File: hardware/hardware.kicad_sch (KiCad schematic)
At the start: 28 parts, among them J1 Conn_01x02, J2 Conn_01x02, P1 USB_C_Plug, Q1 BSS138, Q2 BSS138, U1 ATmega328-P, U3 LM1117S-3.3, U4 CH340C, Y1 Crystal_GND24

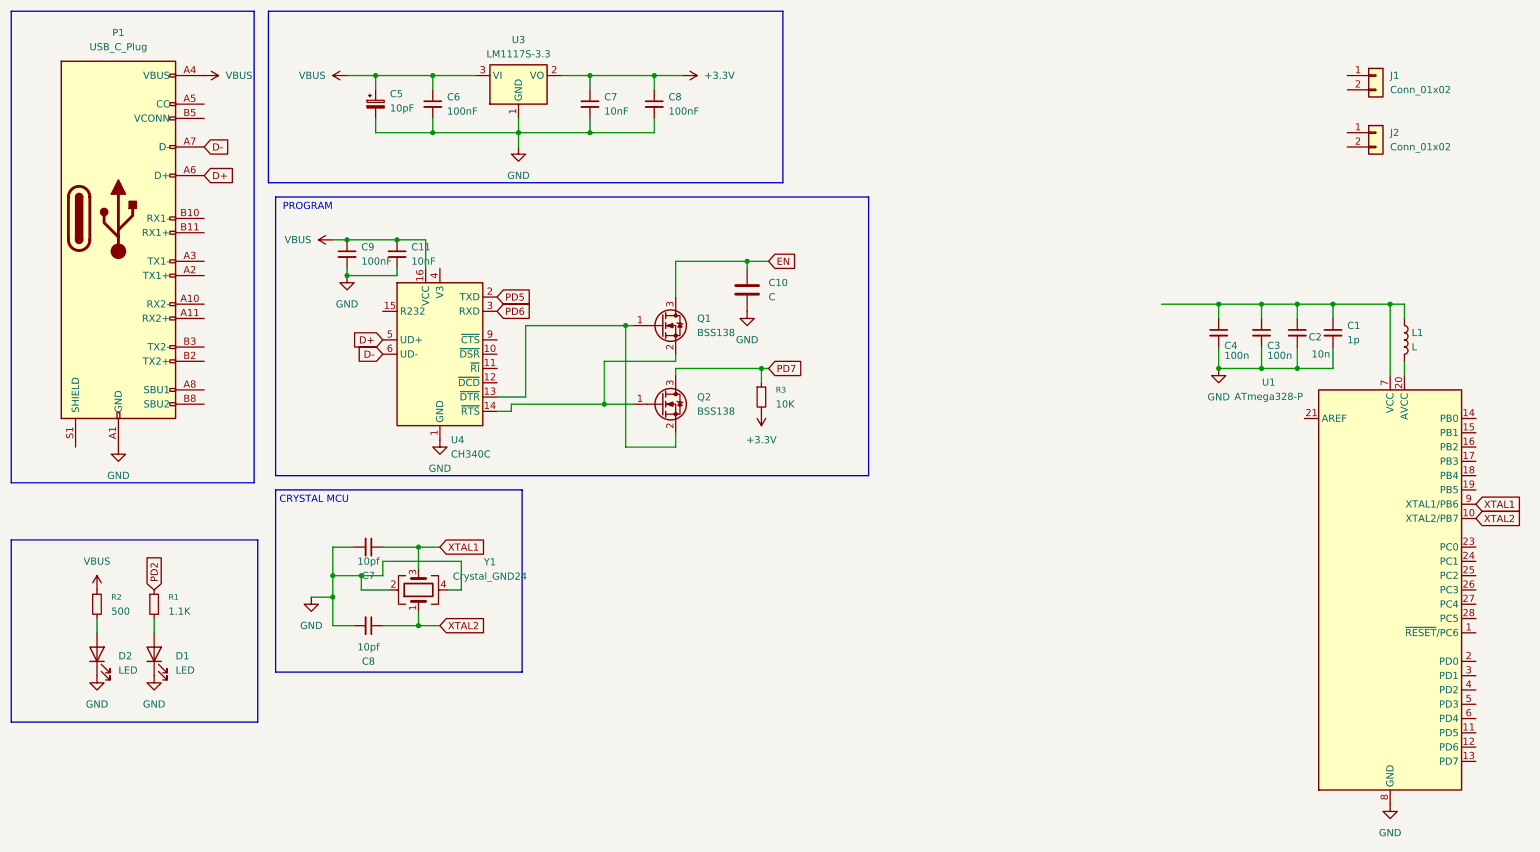
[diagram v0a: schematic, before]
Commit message: add qfn32 atmega
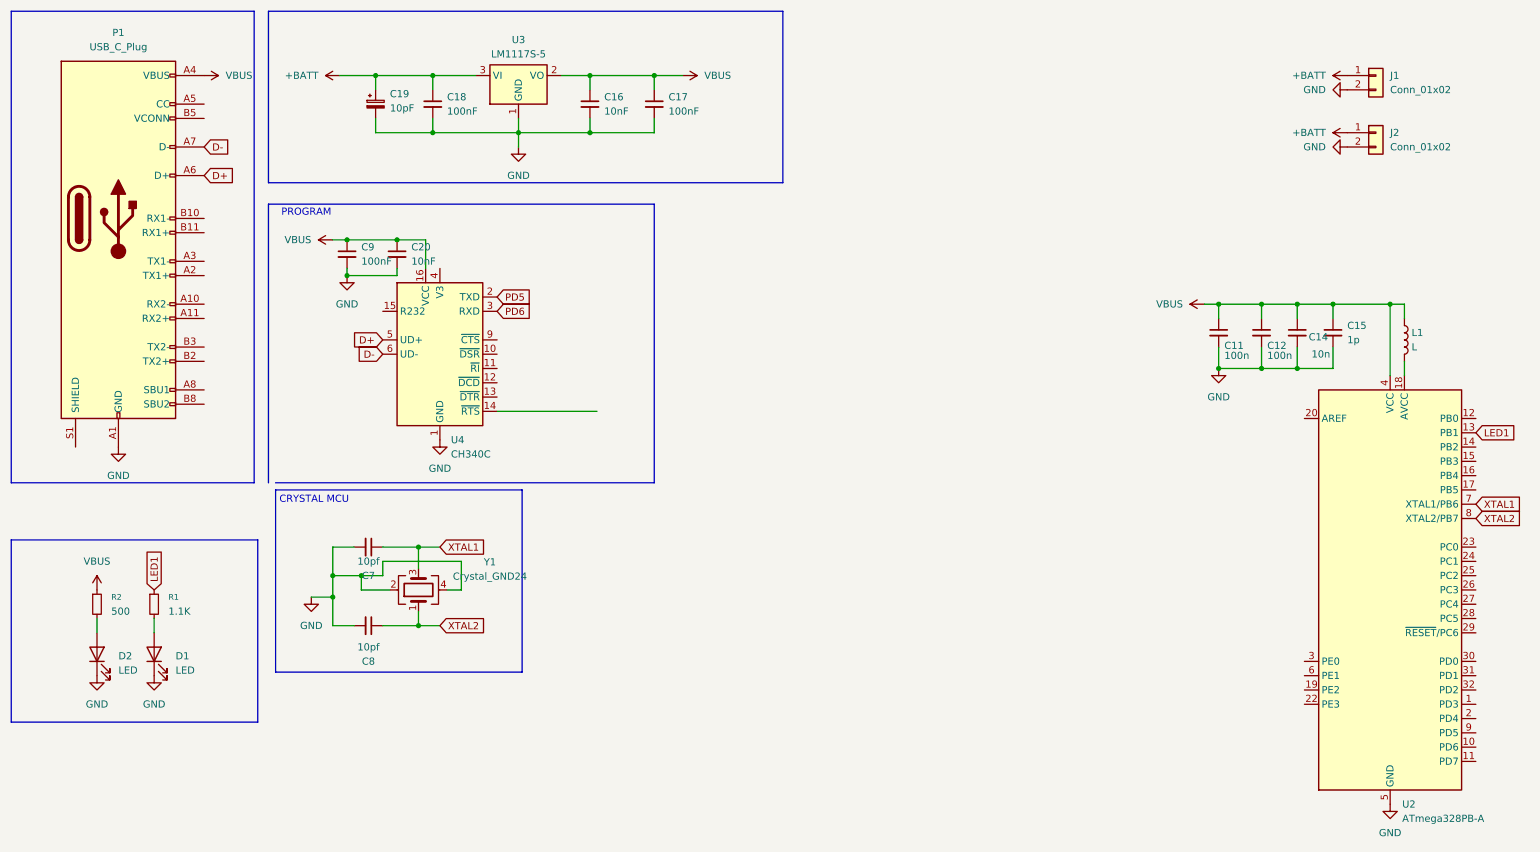
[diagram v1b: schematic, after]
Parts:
- removed C10: C, Capacitor_SMD:C_0603_1608Metric, symbol Device:C
- removed Q1, Q2: BSS138, Package_TO_SOT_SMD:SOT-23, symbol Transistor_FET:BSS138
- removed R3: 10K, Resistor_SMD:R_0603_1608Metric, symbol Device:R_Small
- removed U1: ATmega328-P, Package_DIP:DIP-28_W7.62mm, symbol MCU_Microchip_ATmega:ATmega328-P
- added U2: ATmega328PB-A, Package_QFP:TQFP-32_7x7mm_P0.8mm, symbol MCU_Microchip_ATmega:ATmega328PB-A
- U3: value LM1117S-3.3 -> LM1117S-5
- renumbered C4 to C11, C3 to C12, C2 to C14, C1 to C15, C7 to C16, C8 to C17, C6 to C18, C5 to C19, C11 to C20
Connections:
- net +3.3V is gone; now on net VBUS: C16.1, C17.1, U3.2 (VO)
- net GND: now also J1.2 (Pin_2), J2.2 (Pin_2), U2.21 (GND), U2.5 (GND)
- net VBUS: now also C11.1, C12.1, C14.1, C15.1, L1.1, U2.4 (VCC); no longer C18.1, C19.1, U3.3 (VI)
- net XTAL1: now also U2.7 (XTAL1/PB6)
- net XTAL2: now also U2.8 (XTAL2/PB7)
- net +BATT: now reaches J2.1 (Pin_1)
- net +BATT: now also C18.1, C19.1, J1.1 (Pin_1), U3.3 (VI)
- net at L1.2: now also U2.18 (AVCC)
- net PD2 renamed LED1
- net LED1: now also U2.13 (PB1)

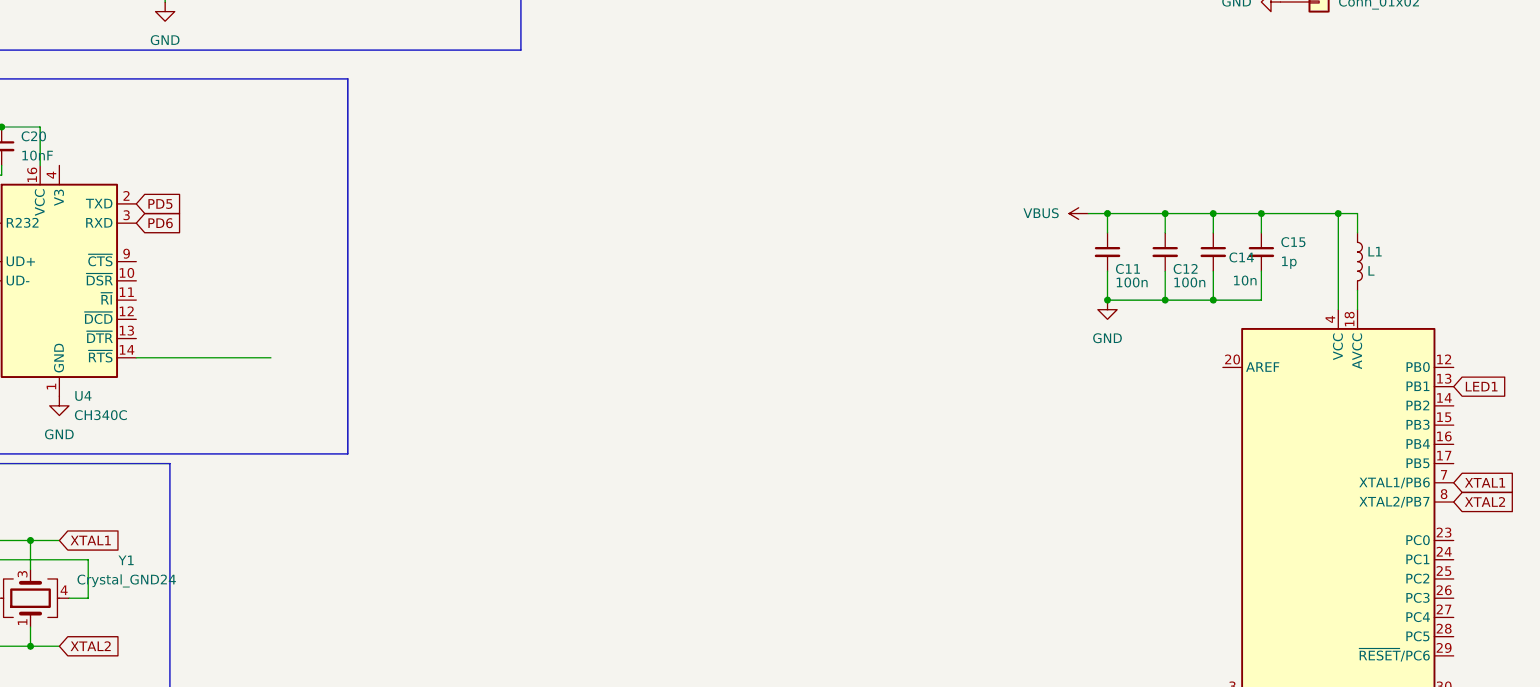
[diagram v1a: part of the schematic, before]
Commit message: add isp connector
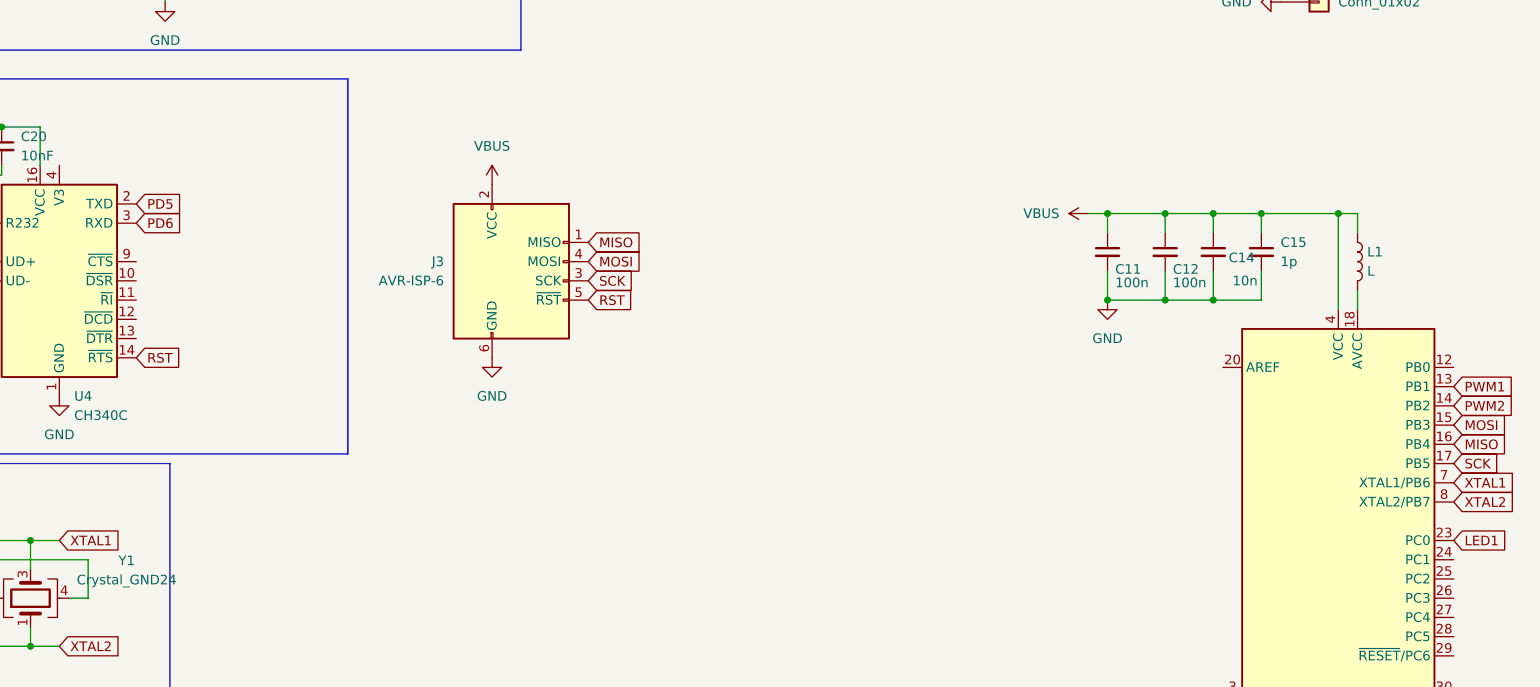
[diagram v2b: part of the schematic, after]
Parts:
- added J3: AVR-ISP-6, Connector_PinHeader_2.54mm:PinHeader_2x03_P2.54mm_Vertical, symbol Connector:AVR-ISP-6
- C11, C12, C14, C15: footprint (none) -> Capacitor_SMD:C_0603_1608Metric
- L1: footprint (none) -> Inductor_SMD:L_0603_1608Metric
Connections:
- net GND: now also J3.6 (GND)
- net LED1: now also U2.23 (PC0); no longer U2.13 (PB1)
- net VBUS: now also J3.2 (VCC)
- net PWM2: now reaches U2.14 (PB2)
- net MOSI: now reaches U2.15 (PB3)
- net MOSI: now also J3.4 (MOSI)
- net MISO: now reaches U2.16 (PB4)
- net MISO: now also J3.1 (MISO)
- net SCK: now reaches U2.17 (PB5)
- net SCK: now also J3.3 (SCK)
- net RST: now reaches U4.14 (~{RTS})
- net RST: now also J3.5 (~{RST})
- new net PWM1: U2.13 (PB1)

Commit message: finish schematic
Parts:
- added J4, J5: Conn_01x03_Pin, Connector_PinHeader_2.54mm:PinHeader_1x03_P2.54mm_Vertical, symbol Connector:Conn_01x03_Pin
- added R3, R4: R_Variable, Potentiometer_THT:Potentiometer_Runtron_RM-065_Vertical, symbol Device:R_Variable
- added R5, R6: 10K, Resistor_SMD:R_0603_1608Metric, symbol Device:R_Small
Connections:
- net GND: now also J4.3 (Pin_3), J5.3 (Pin_3), R5.2, R6.2
- net PWM1: now also J5.2 (Pin_2)
- net PWM2: now also J4.2 (Pin_2)
- net VBUS: now also J4.1 (Pin_1), J5.1 (Pin_1), R3.1, R4.1
- net ADC2: now reaches U2.25 (PC2)
- net ADC2: now also R4.2, R5.1
- net ADC1: now reaches U2.26 (PC3)
- net ADC1: now also R3.2, R6.1

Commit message: pcb wiring
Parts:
- removed R3, R4: R_Variable, Potentiometer_THT:Potentiometer_Runtron_RM-065_Vertical, symbol Device:R_Variable
- removed R5, R6: 10K, Resistor_SMD:R_0603_1608Metric, symbol Device:R_Small
- added RV1, RV2: R_Potentiometer_Trim, Potentiometer_THT:Potentiometer_Runtron_RM-065_Vertical, symbol Device:R_Potentiometer_Trim
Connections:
- net +BATT: now also J1.2 (Pin_2), J2.2 (Pin_2); no longer J1.1 (Pin_1), J2.1 (Pin_1)
- net ADC1: now also RV1.2
- net ADC2: now also RV2.2
- net GND: now also J1.1 (Pin_1), J2.1 (Pin_1), RV1.3, RV2.3; no longer J1.2 (Pin_2), J2.2 (Pin_2)
- net RST: now also U2.29 (~{RESET}/PC6)
- net VBUS: now also RV1.1, RV2.1
